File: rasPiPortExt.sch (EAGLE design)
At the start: 15 parts, among them IC1 MCP2300X/P, IC2 74LVC1G07DCK, IC3 74LVC1G07DCK, T1 BSS138PWWAVE, T2 BSS138PWWAVE, X3 SSW-103-02-S-T, X4 SSW-108-02-S-T

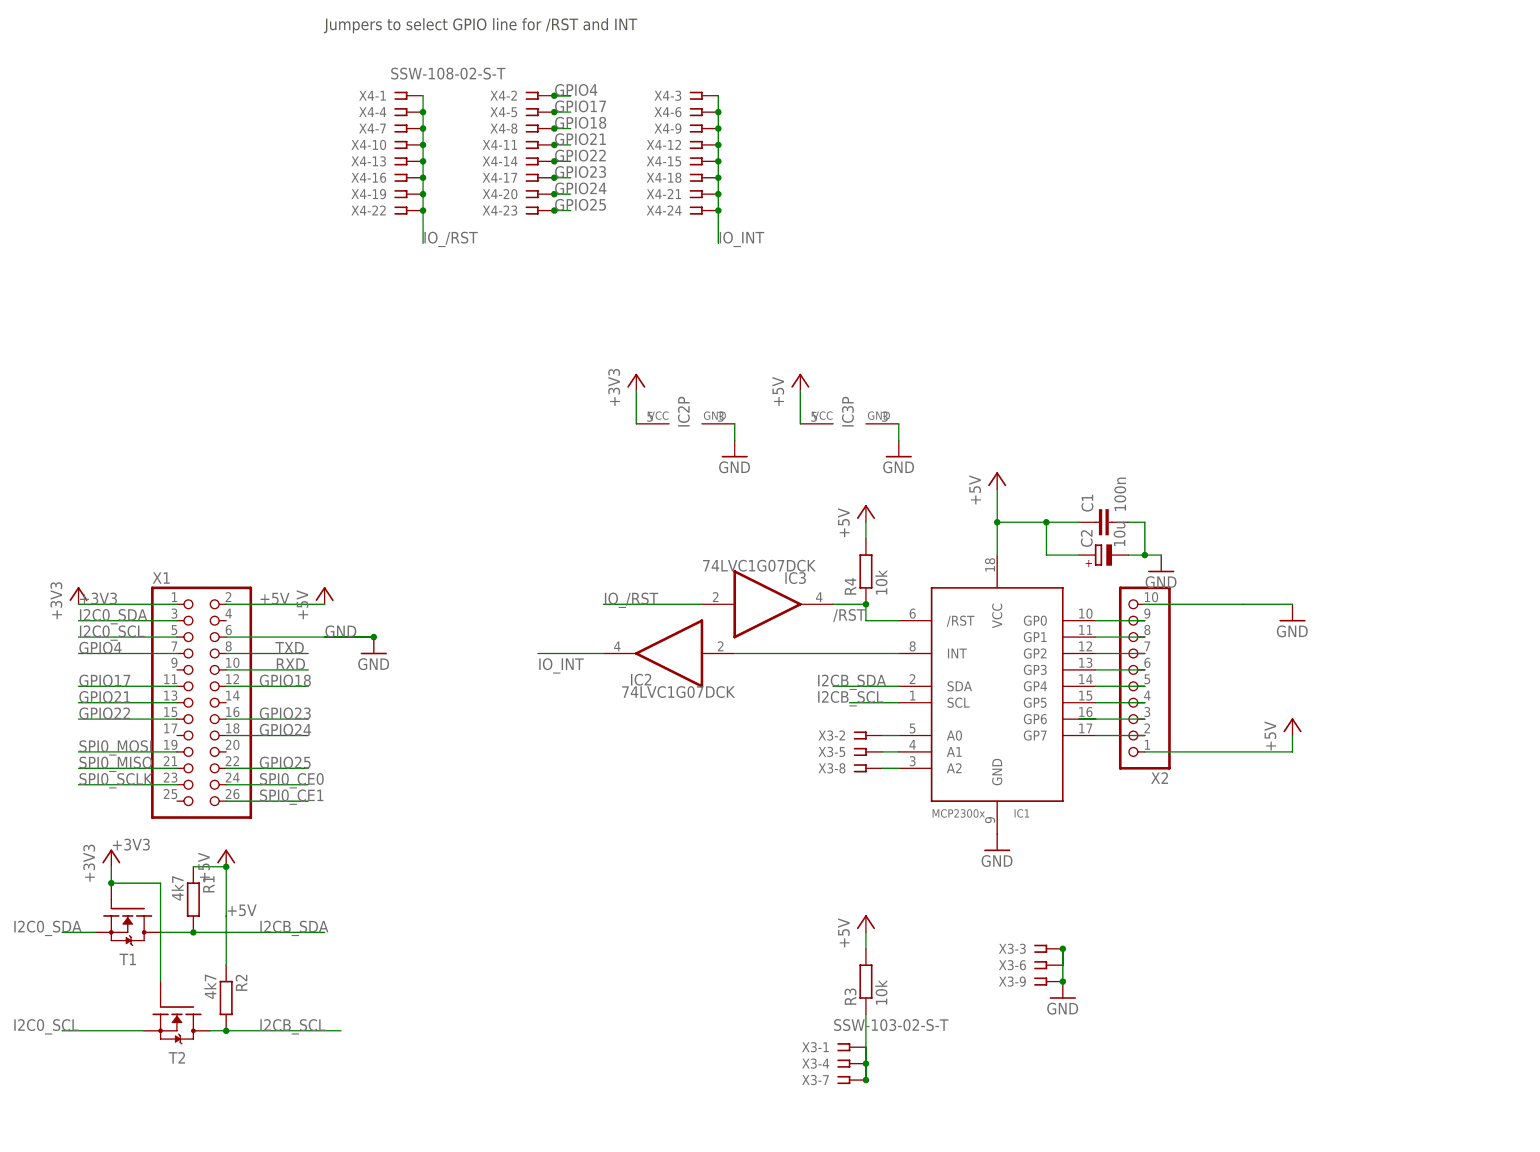
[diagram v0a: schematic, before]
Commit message: changed design for /RST line, added additional R rearranged some components and traces v1.1 submitted for etching
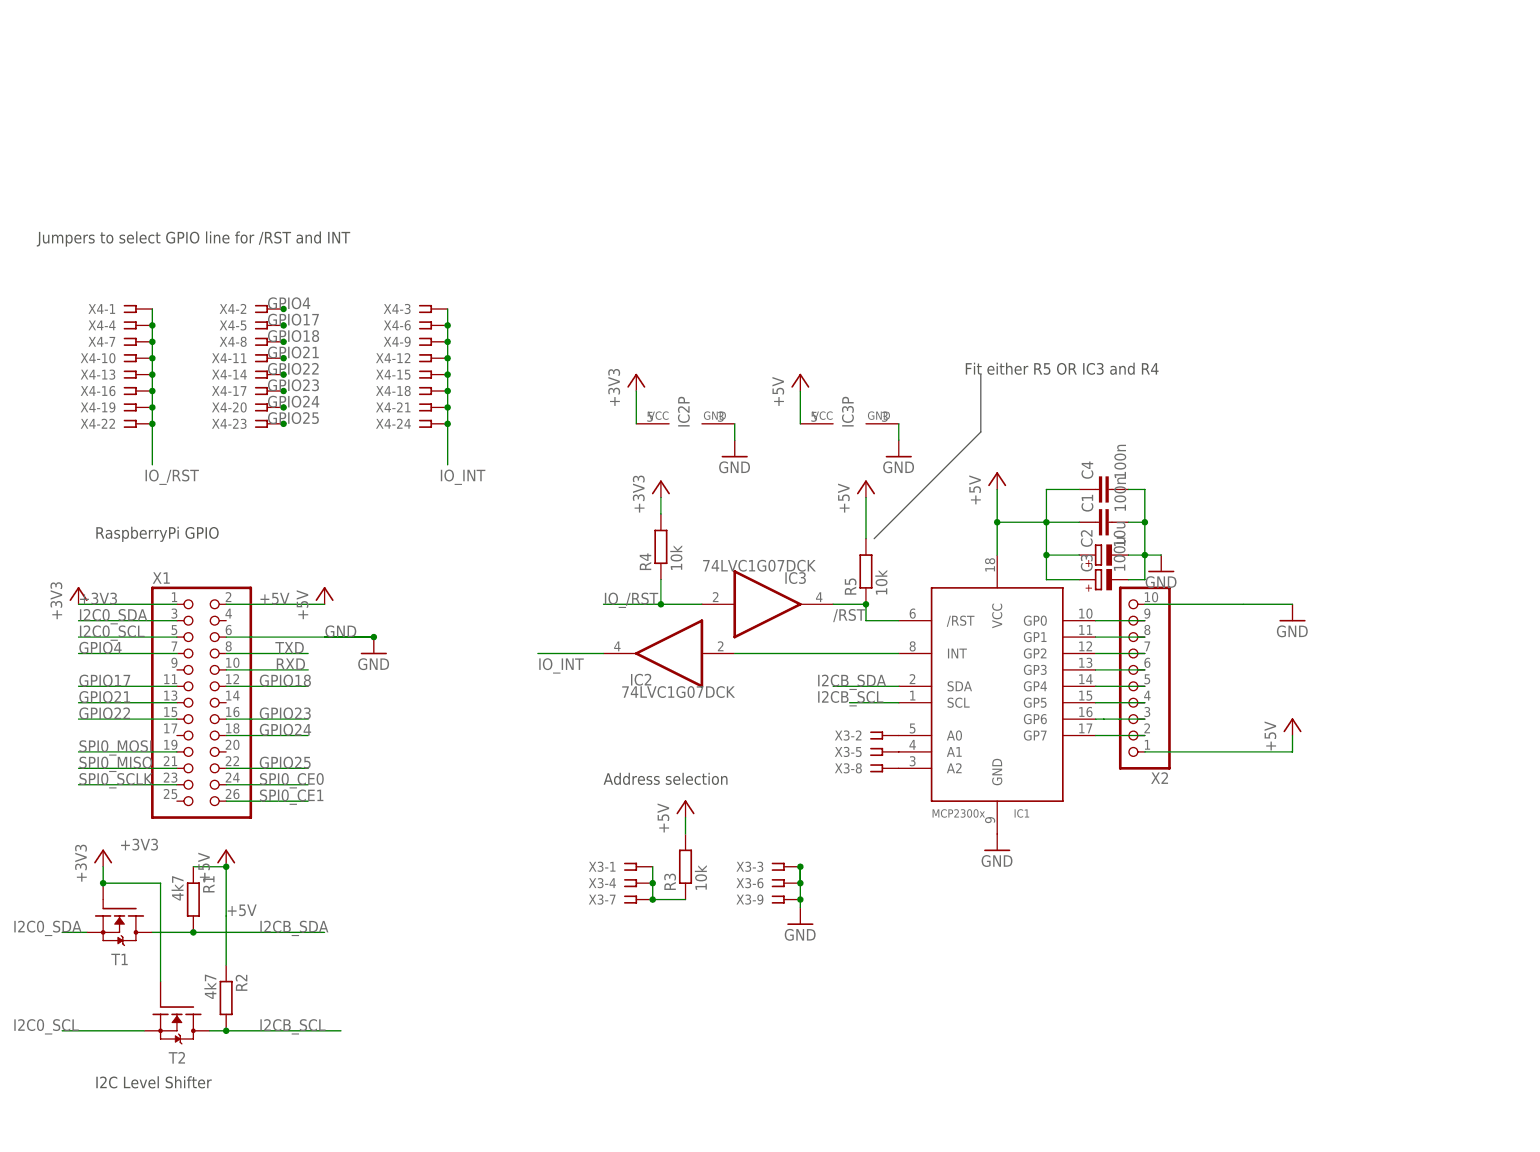
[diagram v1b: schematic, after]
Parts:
- added C3: 100u, resistor:CPOL-EUE2.5-5
- added C4: 100n, resistor:C-EU050-025X075
- added R5: 10k, smdParts:R-EU_R1206
- R1, R2: device smdParts:R-EU_R0603 -> smdParts:R-EU_R1206
- R3, R4: device smdParts:R-EU_R0805 -> smdParts:R-EU_R1206
- T1, T2: value BSS138PWWAVE -> BSS138PW"; device smdParts:BSS138PWWAVE -> smdParts:BSS138PW"
- X3: device con-samtec:SSW-103-02-S-T -> SD:SSW-103-02-S-T
- X4: value SSW-108-02-S-T -> (none); device con-samtec:SSW-108-02-S-T -> SD:SSW-108-02-S-T
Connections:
- net +3V3: now also R4.2
- net +5V: now also C3.+, C4.1, R5.2; no longer R4.2
- net /RST: now also R5.1; no longer R4.1
- net GND: now also C3.-, C4.2
- net IO_/RST: now also R4.1
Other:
- note added: "Address selection"
- note added: "Fit either R5 OR IC3 and R4"
- note added: "I2C Level Shifter"
- note added: "RaspberryPi GPIO"
- moved on the sheet: R3, R4, T1, X3-1, X3-2, X3-3, X3-4, X3-5, X3-6, X3-7, X3-8, X3-9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

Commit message: improved buffer for IRQ line, adding protection resistor
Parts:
- removed IC3: 74LVC1G07DCK, 74xx-little-us:74LVC1G07DCK
- added R6: 1k, smdParts:R-EU_R0805
- added T3: BSS138PW", smdParts:BSS138PW"
- R1, R2, R3, R4, R5: device smdParts:R-EU_R1206 -> smdParts:R-EU_R0805
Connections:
- new net N$13: IC2A.O, R6.1
- net +3V3: now also T3.G
- net +5V: no longer IC3P.VCC
- net /RST: now also T3.D; no longer IC3A.O
- net GND: no longer IC3P.GND
- net IO_/RST: now also T3.S; no longer IC3A.I
- net IO_INT: now also R6.2; no longer IC2A.O
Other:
- note added: "Jonas Zimmermann"
- note removed: "Fit either R5 OR IC3 and R4"
- moved on the sheet: R4
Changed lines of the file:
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@@
 <part name="P+3" library="supply1" deviceset="+5V" device=""/>
 <part name="GND3" library="supply1" deviceset="GND" device=""/>
-<part name="R3" library="smdParts" deviceset="R-EU_" device="R1206" value="10k"/>
+<part name="R3" library="smdParts" deviceset="R-EU_" device="R0805" value="10k"/>
 <part name="P+5" library="supply1" deviceset="+5V" device=""/>
-<part name="R1" library="smdParts" deviceset="R-EU_" device="R1206" value="4k7"/>
-<part name="R2" library="smdParts" deviceset="R-EU_" device="R1206" value="4k7"/>
+<part name="R1" library="smdParts" deviceset="R-EU_" device="R0805" value="4k7"/>
+<part name="R2" library="smdParts" deviceset="R-EU_" device="R0805" value="4k7"/>
 <part name="+3V1" library="supply1" deviceset="+3V3" device=""/>
 <part name="+3V2" library="supply1" deviceset="+3V3" device=""/>
@@
 <part name="+3V3" library="supply1" deviceset="+3V3" device=""/>
 <part name="GND6" library="supply1" deviceset="GND" device=""/>
-<part name="R4" library="smdParts" deviceset="R-EU_" device="R1206" value="10k"/>
-<part name="IC3" library="74xx-little-us" deviceset="74*1G07" device="DCK" technology="LVC"/>
-<part name="P+7" library="supply1" deviceset="+5V" device=""/>
-<part name="GND7" library="supply1" deviceset="GND" device=""/>
+<part name="R4" library="smdParts" deviceset="R-EU_" device="R0805" value="10k"/>
 <part name="+3V4" library="supply1" deviceset="+3V3" device=""/>
 <part name="C3" library="resistor" deviceset="CPOL-EU" device="E2.5-5" value="100u"/>
 <part name="C4" library="resistor" deviceset="C-EU" device="050-025X075" value="100n"/>
-<part name="R5" library="smdParts" deviceset="R-EU_" device="R1206" value="10k"/>
+<part name="R5" library="smdParts" deviceset="R-EU_" device="R0805" value="10k"/>
 <part name="P+6" library="supply1" deviceset="+5V" device=""/>
+<part name="FRAME1" library="frames" deviceset="A4L-LOC" device="" value="Jonas"/>
+<part name="T3" library="smdParts" deviceset="BSS138PW" device="&quot;"/>
+<part name="R6" library="smdParts" deviceset="R-EU_" device="R0805" value="1k"/>
 </parts>
 <sheets>
@@
 <text x="-73.66" y="88.9" size="1.778" layer="97">RaspberryPi GPIO</text>
 <text x="-73.66" y="3.81" size="1.778" layer="97">I2C Level Shifter</text>
-<frame x1="-113.03" y1="-29.21" x2="128.27" y2="152.4" columns="8" rows="5" layer="94"/>
-<text x="60.96" y="114.3" size="1.778" layer="97">Fit either R5 OR IC3 and R4</text>
-<wire x1="63.5" y1="114.3" x2="63.5" y2="105.41" width="0.1524" layer="97"/>
-<wire x1="63.5" y1="105.41" x2="46.99" y2="88.9" width="0.1524" layer="97"/>
+<text x="109.22" y="-2.54" size="2.54" layer="94">Jonas Zimmermann</text>
 </plain>
 <instances>
@@
 <instance part="+3V3" gate="G$1" x="10.16" y="114.3"/>
 <instance part="GND6" gate="1" x="25.4" y="101.6"/>
-<instance part="R4" gate="G$1" x="13.97" y="87.63" rot="R90"/>
-<instance part="IC3" gate="A" x="30.48" y="78.74" smashed="yes">
-<attribute name="NAME" x="33.02" y="81.915" size="1.778" layer="95"/>
-<attribute name="VALUE" x="20.32" y="83.82" size="1.778" layer="96"/>
-</instance>
-<instance part="IC3" gate="P" x="43.18" y="106.68" rot="R90"/>
-<instance part="P+7" gate="1" x="35.56" y="114.3"/>
-<instance part="GND7" gate="1" x="50.8" y="101.6"/>
-<instance part="+3V4" gate="G$1" x="13.97" y="97.79"/>
+<instance part="R4" gate="G$1" x="24.13" y="86.36" rot="R90"/>
+<instance part="+3V4" gate="G$1" x="24.13" y="97.79"/>
 <instance part="C3" gate="G$1" x="81.28" y="82.55" rot="R90"/>
 <instance part="C4" gate="G$1" x="81.28" y="96.52" rot="R90"/>
 <instance part="R5" gate="G$1" x="45.72" y="83.82" rot="R90"/>
 <instance part="P+6" gate="1" x="45.72" y="97.79"/>
+<instance part="FRAME1" gate="G$1" x="-109.22" y="-22.86" smashed="yes">
+<attribute name="DRAWING_NAME" x="107.95" y="-7.62" size="2.54" layer="94" font="vector"/>
+<attribute name="LAST_DATE_TIME" x="107.95" y="-12.7" size="2.286" layer="94" font="vector"/>
+<attribute name="SHEET" x="121.285" y="-17.78" size="2.54" layer="94" font="vector"/>
+</instance>
+<instance part="T3" gate="G$1" x="34.29" y="81.28" smashed="yes" rot="R270">
+<attribute name="NAME" x="33.02" y="73.66" size="1.778" layer="95"/>
+</instance>
+<instance part="R6" gate="G$1" x="-2.54" y="71.12" rot="R180"/>
 </instances>
 <busses>
@@
 <pinref part="GND6" gate="1" pin="GND"/>
 <wire x1="25.4" y1="106.68" x2="25.4" y2="104.14" width="0.1524" layer="91"/>
-</segment>
-<segment>
-<pinref part="IC3" gate="P" pin="GND"/>
-<pinref part="GND7" gate="1" pin="GND"/>
-<wire x1="50.8" y1="104.14" x2="50.8" y2="106.68" width="0.1524" layer="91"/>
 </segment>
 </net>
@@
 </segment>
 <segment>
-<pinref part="IC3" gate="P" pin="VCC"/>
-<pinref part="P+7" gate="1" pin="+5V"/>
-<wire x1="35.56" y1="111.76" x2="35.56" y2="106.68" width="0.1524" layer="91"/>
-</segment>
-<segment>
 <pinref part="R5" gate="G$1" pin="2"/>
 <pinref part="P+6" gate="1" pin="+5V"/>
@@
 <net name="IO_INT" class="0">
 <segment>
-<wire x1="5.08" y1="71.12" x2="-5.08" y2="71.12" width="0.1524" layer="91"/>
-<label x="-5.08" y="68.58" size="1.778" layer="95"/>
-<pinref part="IC2" gate="A" pin="O"/>
+<label x="-13.97" y="72.39" size="1.778" layer="95"/>
+<pinref part="R6" gate="G$1" pin="2"/>
+<wire x1="-7.62" y1="71.12" x2="-11.43" y2="71.12" width="0.1524" layer="91"/>
 </segment>
 <segment>
@@
 </segment>
 <segment>
-<pinref part="IC3" gate="A" pin="I"/>
-<wire x1="20.32" y1="78.74" x2="13.97" y2="78.74" width="0.1524" layer="91"/>
+<wire x1="29.21" y1="78.74" x2="24.13" y2="78.74" width="0.1524" layer="91"/>
 <label x="5.08" y="78.74" size="1.778" layer="95"/>
 <pinref part="R4" gate="G$1" pin="1"/>
-<wire x1="13.97" y1="78.74" x2="5.08" y2="78.74" width="0.1524" layer="91"/>
-<wire x1="13.97" y1="82.55" x2="13.97" y2="78.74" width="0.1524" layer="91"/>
-<junction x="13.97" y="78.74"/>
+<wire x1="24.13" y1="78.74" x2="5.08" y2="78.74" width="0.1524" layer="91"/>
+<wire x1="24.13" y1="81.28" x2="24.13" y2="78.74" width="0.1524" layer="91"/>
+<junction x="24.13" y="78.74"/>
+<pinref part="T3" gate="G$1" pin="S"/>
 </segment>
 </net>
@@
 <pinref part="+3V4" gate="G$1" pin="+3V3"/>
 <pinref part="R4" gate="G$1" pin="2"/>
-<wire x1="13.97" y1="95.25" x2="13.97" y2="92.71" width="0.1524" layer="91"/>
+<wire x1="24.13" y1="95.25" x2="24.13" y2="93.98" width="0.1524" layer="91"/>
+<pinref part="T3" gate="G$1" pin="G"/>
+<wire x1="24.13" y1="93.98" x2="24.13" y2="91.44" width="0.1524" layer="91"/>
+<wire x1="31.75" y1="86.36" x2="31.75" y2="92.71" width="0.1524" layer="91"/>
+<wire x1="31.75" y1="92.71" x2="31.75" y2="93.98" width="0.1524" layer="91"/>
+<wire x1="31.75" y1="93.98" x2="24.13" y2="93.98" width="0.1524" layer="91"/>
+<junction x="24.13" y="93.98"/>
 </segment>
 </net>
@@
 <pinref part="IC1" gate="G$1" pin="/RST"/>
 <label x="40.64" y="76.2" size="1.778" layer="95"/>
-<pinref part="IC3" gate="A" pin="O"/>
 <wire x1="45.72" y1="76.2" x2="50.8" y2="76.2" width="0.1524" layer="91"/>
-<wire x1="40.64" y1="78.74" x2="45.72" y2="78.74" width="0.1524" layer="91"/>
+<wire x1="39.37" y1="78.74" x2="45.72" y2="78.74" width="0.1524" layer="91"/>
 <wire x1="45.72" y1="78.74" x2="45.72" y2="76.2" width="0.1524" layer="91"/>
 <pinref part="R5" gate="G$1" pin="1"/>
 <junction x="45.72" y="78.74"/>
-</segment>
-</net>
+<pinref part="T3" gate="G$1" pin="D"/>
+</segment>
+</net>
+<net name="N$13" class="0">
+<segment>
+<pinref part="IC2" gate="A" pin="O"/>
+<pinref part="R6" gate="G$1" pin="1"/>
+<wire x1="2.54" y1="71.12" x2="5.08" y2="71.12" width="0.1524" layer="91"/>
+</segment>
+</net>
